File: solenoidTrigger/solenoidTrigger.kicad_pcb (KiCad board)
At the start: 2 copper layers, 88.9 x 88.9 mm, 45 parts, among them J8 CONN_02X03, P1 OSTTC03, P2 OSTTC02, P3 OSTTC08, P4 OSTTC03, P5 OSTTC03, Q1 NMOS_CDS16, Q2 NMOS_CDS16, Q3 NMOS_CDS16, Q4 NMOS_CDS16, Q5 NMOS_CDS16, Q6 NMOS_CDS16, U1 L78M05CDT-TR, U2 ATmega328P-AU, Y2 Crystal_SMD

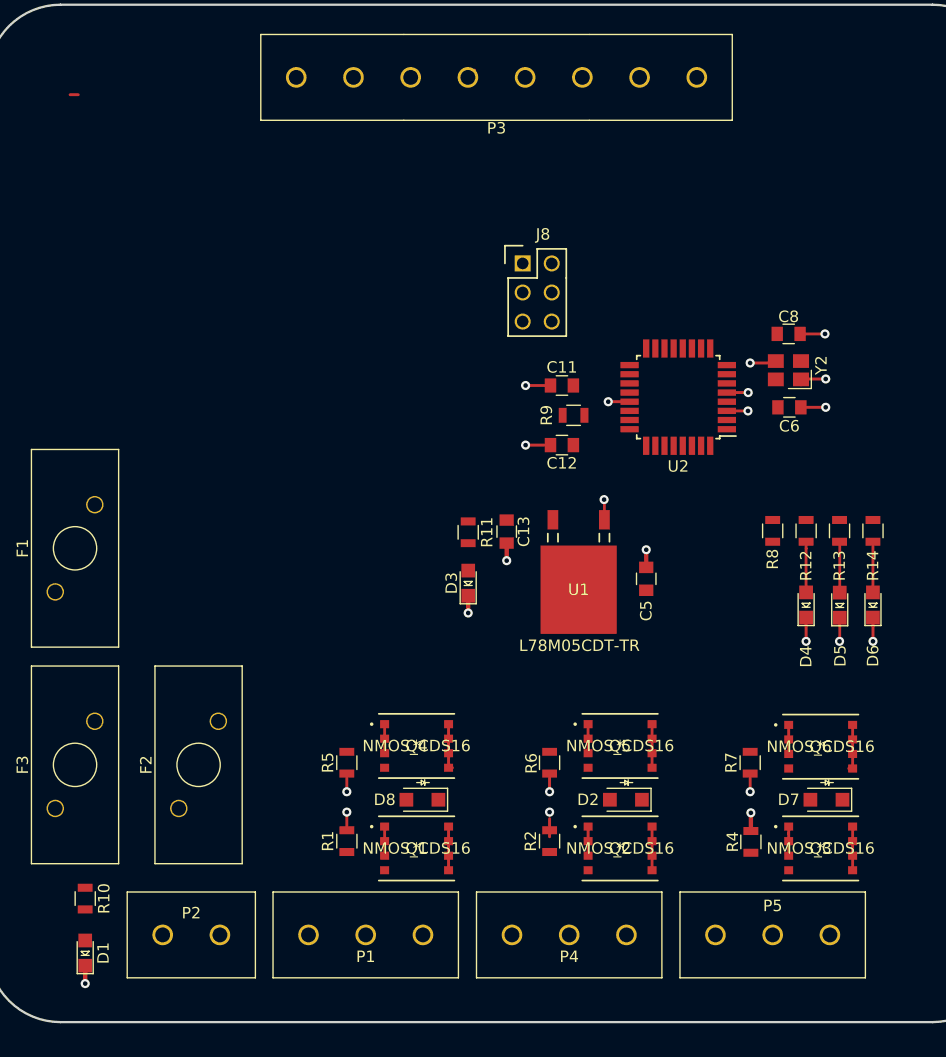
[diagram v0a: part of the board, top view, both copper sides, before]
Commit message: global deletion of all tracks so I can replace all of them
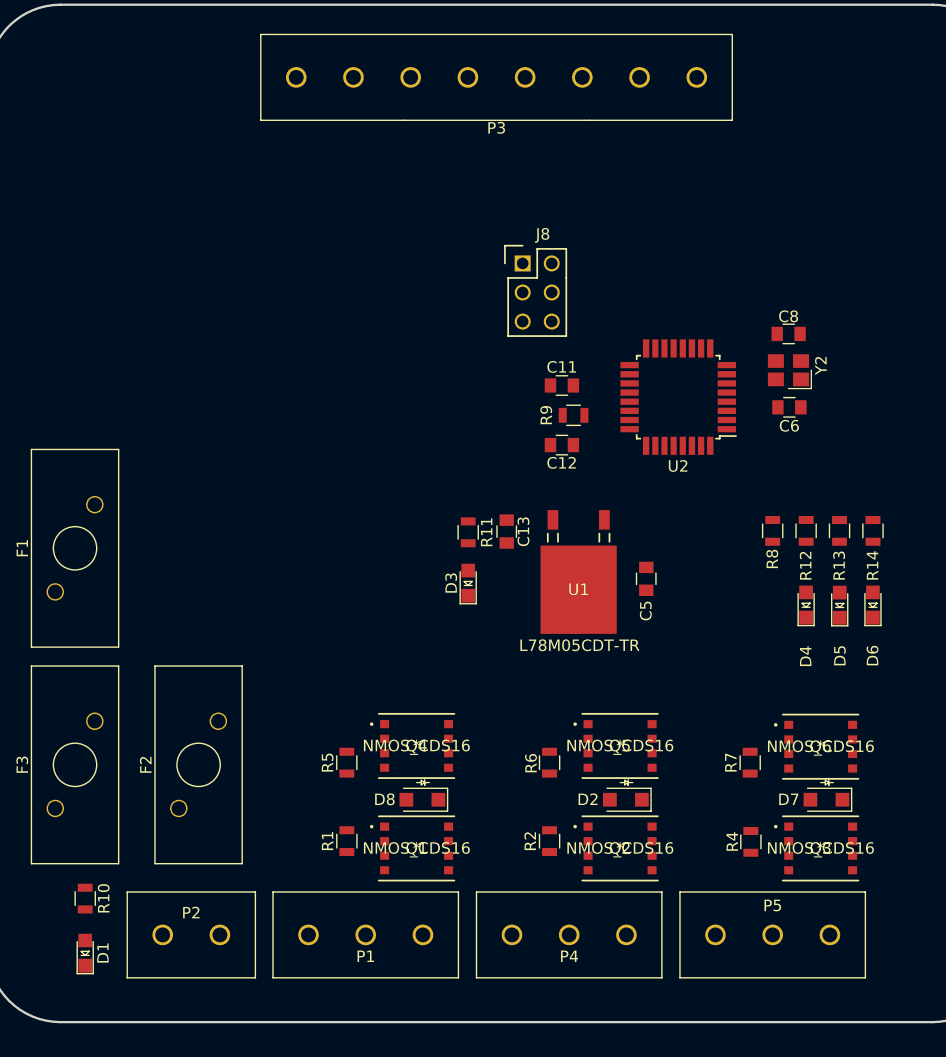
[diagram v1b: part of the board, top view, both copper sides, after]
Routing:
- net GND: track 43.3 -> 0.00 mm, vias 23 -> 0
- net /12V_Switch: track 23.7 -> 0.00 mm
- net /12V_Solenoid3: track 5.08 -> 0.00 mm
- net /12V_Solenoid2: track 5.08 -> 0.00 mm
- net /12V_Solenoid1: track 5.08 -> 0.00 mm
- net Net-(D5-Pad2): track 4.79 -> 0.00 mm
- net Net-(D6-Pad2): track 4.43 -> 0.00 mm
- net Net-(D4-Pad2): track 4.43 -> 0.00 mm
- net /MISO: track 1.41 -> 0.00 mm
- net (no net): track 0.72 -> 0.00 mm
- net VCC: track 0.58 -> 0.00 mm
- net /ctrl_pin_1-2: track 0.53 -> 0.00 mm
- net /PLED3: track 0.53 -> 0.00 mm

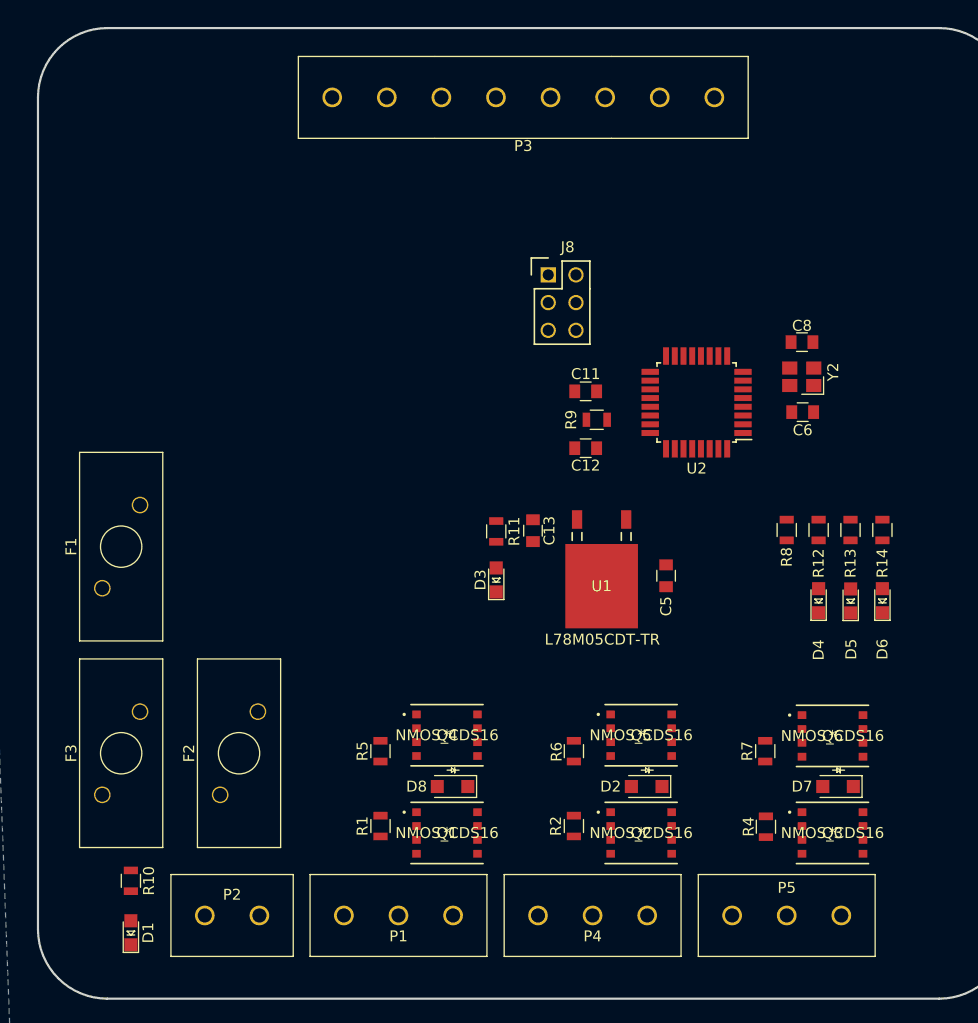
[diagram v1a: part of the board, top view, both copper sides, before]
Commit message: placed down about half the traces
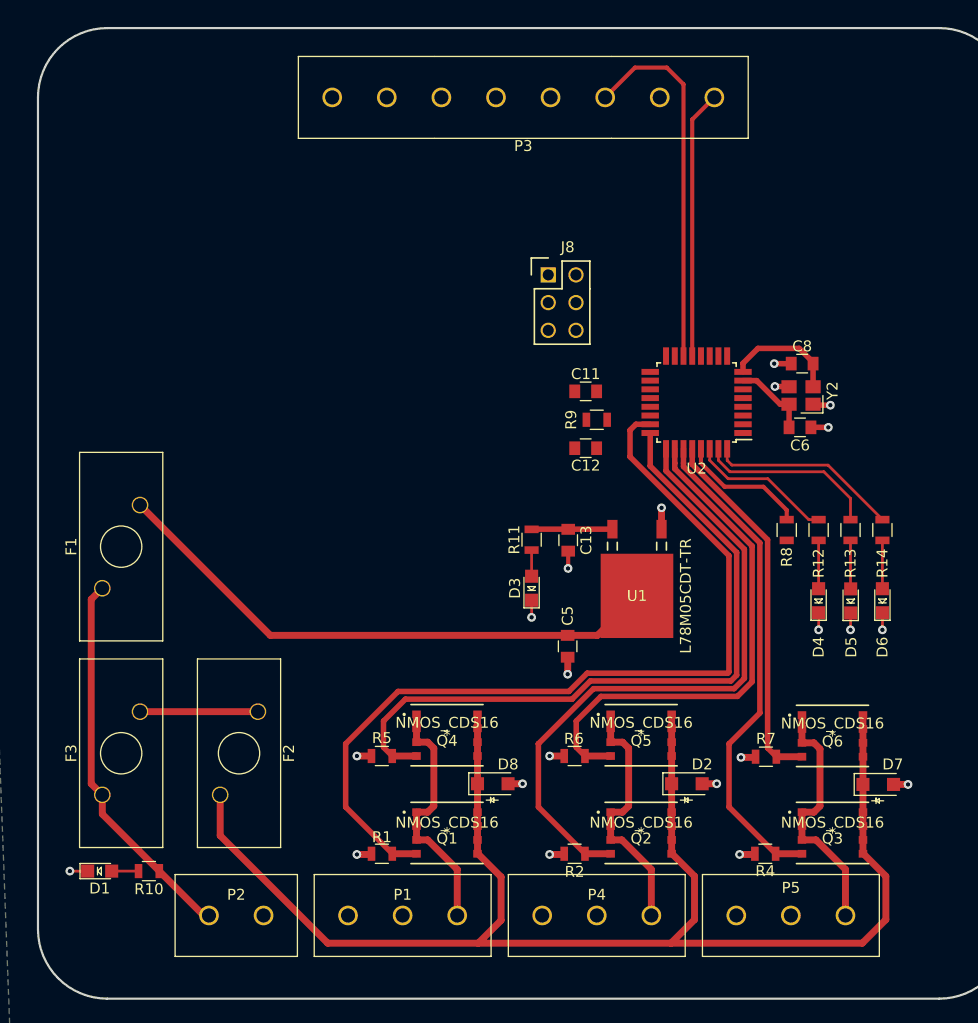
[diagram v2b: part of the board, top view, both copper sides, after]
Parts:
- moved F2 22.4 mm to (121.3, 127.1), turned to 180 degrees
- moved C5 11.1 mm to (151.4, 106.2), turned to 90 degrees
- moved D1 6.33 mm to (108.5, 126.7), turned to 0 degrees
- moved D2 3.69 mm to (162.3, 118.7), turned to 0 degrees
- moved D8 3.69 mm to (144.5, 118.7), turned to 0 degrees
- moved D7 3.69 mm to (179.8, 118.8), turned to 0 degrees
- moved U1 3.36 mm to (157.7, 101.5)
- moved C13 3.34 mm to (151.4, 96.4)
- moved D3 3.33 mm to (148.1, 100.8)
- moved R11 3.33 mm to (148.1, 96.4)
- moved R1 2.54 mm to (134.4, 125.2), turned to 180 degrees
- moved R2 2.54 mm to (152.0, 125.2), turned to 180 degrees
- moved R4 2.48 mm to (169.5, 125.2), turned to 180 degrees
- moved C8 1.97 mm to (172.9, 80.3), turned to 180 degrees
- moved R10 1.88 mm to (113.0, 126.7), turned to 180 degrees
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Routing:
- net /12V_Switch: track 0.00 -> 134.8 mm
- net /ctrl_pin_1-1: track 0.00 -> 79.9 mm
- net /ctrl_pin_1-2: track 0.00 -> 65.3 mm
- net /ctrl_pin_2-1: track 0.00 -> 59.5 mm
- net /12V_Low: track 0.00 -> 52.0 mm
- net /ctrl_pin_2-2: track 0.00 -> 47.8 mm
- net /ctrl_pin_3-1: track 0.00 -> 45.3 mm
- net /Source(12V): track 0.00 -> 35.1 mm
- net /CS: track 0.00 -> 33.8 mm
- net /ctrl_pin_3-2: track 0.00 -> 33.7 mm
- net GND: track 0.00 -> 31.3 mm, vias 0 -> 21
- net /G0(IRQ): track 0.00 -> 24.5 mm
- net /12V_Solenoid1: track 0.00 -> 23.1 mm
- net /12V_Solenoid2: track 0.00 -> 23.1 mm
- net /12V_Solenoid3: track 0.00 -> 23.0 mm
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
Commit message: first pass done pending approval
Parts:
- added REF**: Mounting_Hole_4-40, footprints:Mounting_Hole_4-40, F.Cu at (114.8, 44.5)
- added REF**: Mounting_Hole_4-40, footprints:Mounting_Hole_4-40, F.Cu at (184.4, 131.2)
- added REF**: Mounting_Hole_4-40, footprints:Mounting_Hole_4-40, F.Cu at (184.4, 56.9)
- added REF**: Mounting_Hole_4-40, footprints:Mounting_Hole_4-40, F.Cu at (110.5, 131.2)
- moved D3 0.38 mm to (148.5, 100.8)
- moved R11 0.38 mm to (148.5, 96.4)
- moved C13 0.25 mm to (151.7, 96.4)
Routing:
- net VCC: track 7.41 -> 160.0 mm, vias 0 -> 8
- net /RESET: track 11.8 -> 125.5 mm, vias 0 -> 4
- net /SCK: track 0.00 -> 52.0 mm
- net /MISO: track 0.00 -> 50.9 mm
- net /MOSI: track 0.00 -> 41.5 mm, vias 0 -> 2
- net GND: track 31.3 -> 39.9 mm, vias 21 -> 26
- net Net-(C11-Pad2): track 0.00 -> 8.31 mm

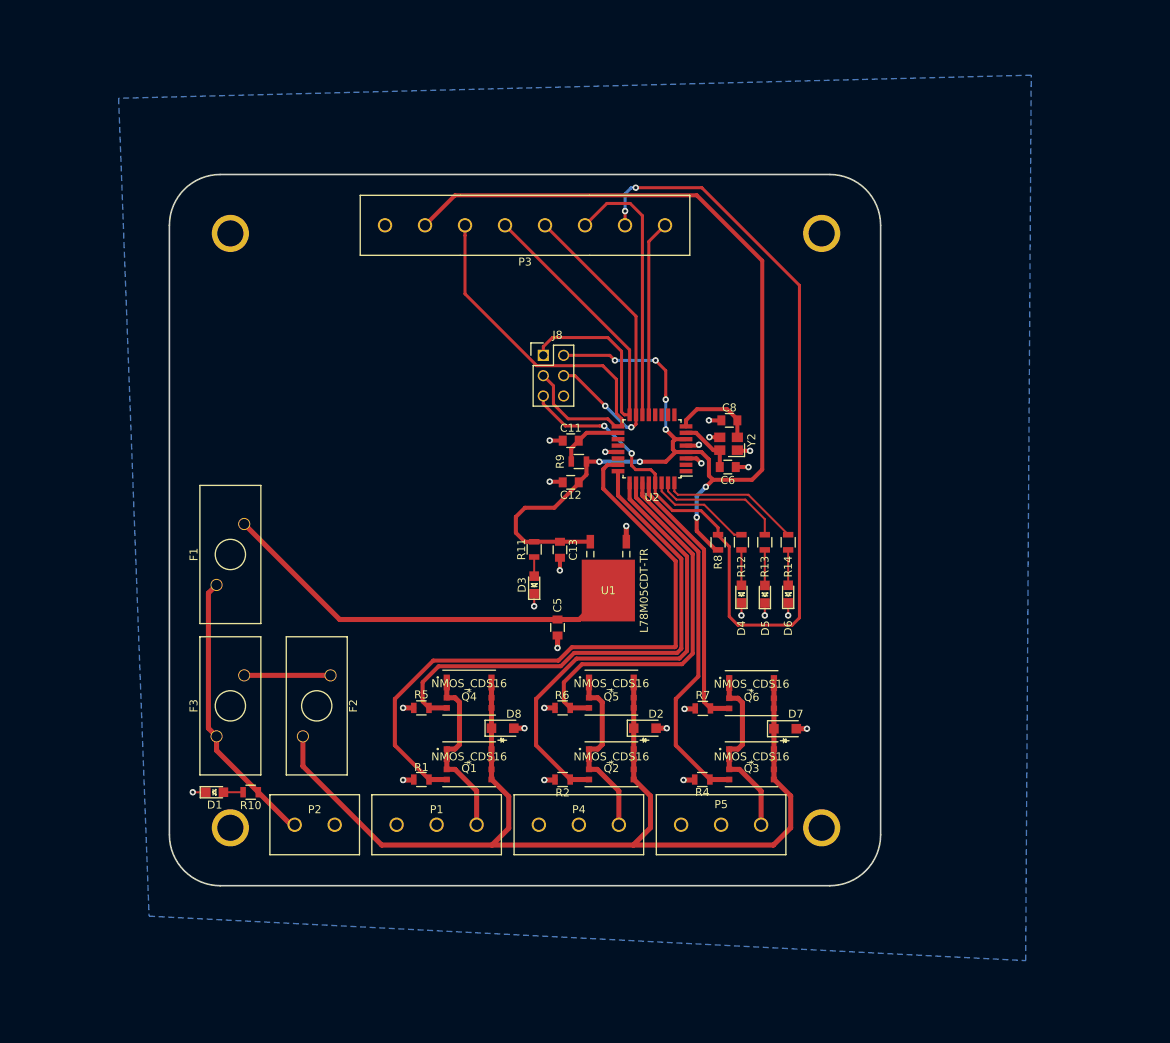
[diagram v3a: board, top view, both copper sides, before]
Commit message: added another LED, changed some pins, changed flybacks
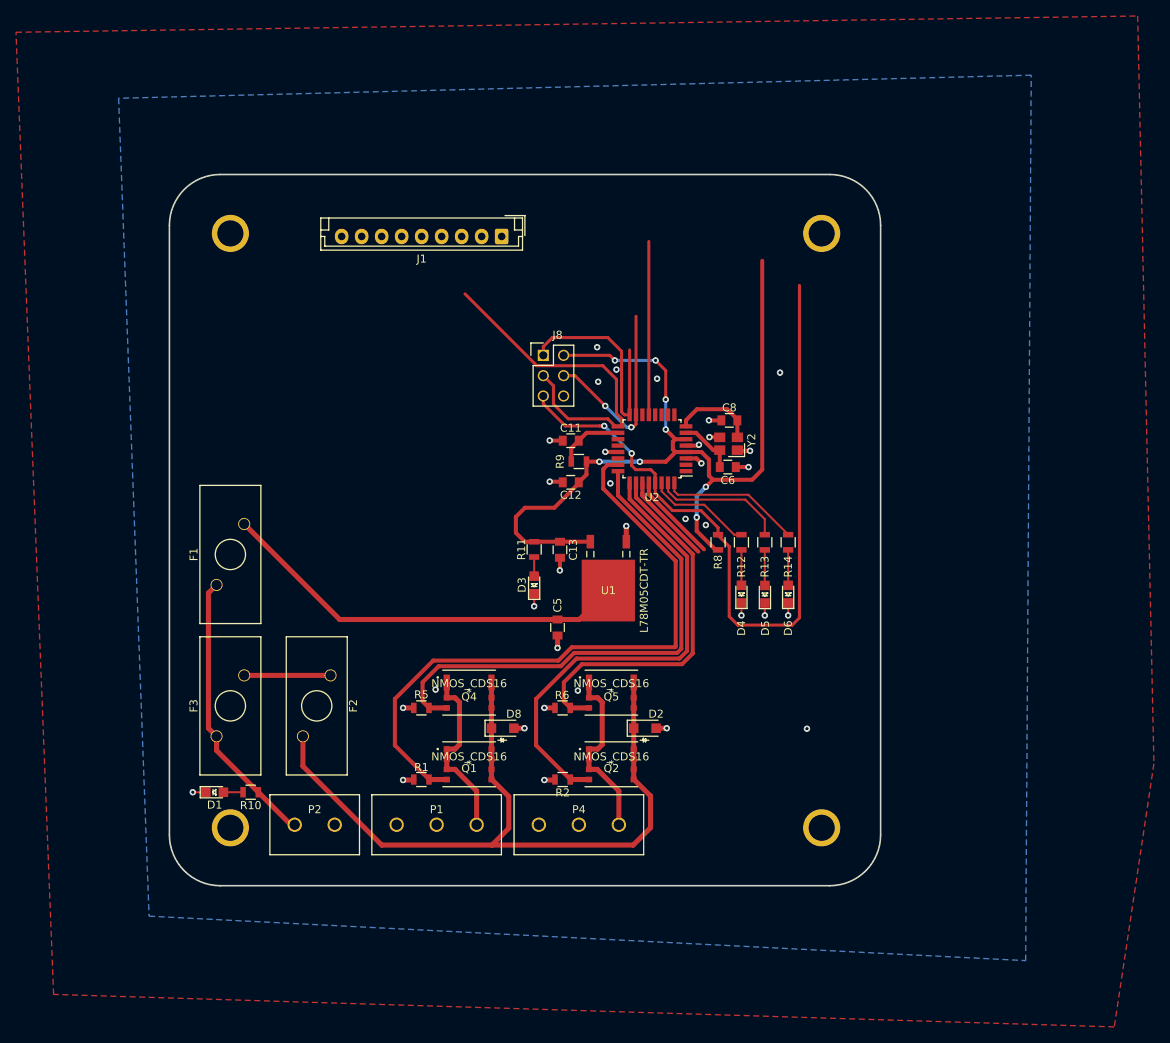
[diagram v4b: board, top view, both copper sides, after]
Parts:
- removed D7: SS110LW, footprints:D_SOD-123W_OEM
- removed P3: OSTTC08, footprints:OSTTC080162
- removed P5: OSTTC03, footprints:OSTTC030162
- removed Q3, Q6: NMOS_CDS16, footprints:CSD16322Q5
- removed R4, R7: R_1K, footprints:R_0805_OEM
- added J1: Conn_01x09_Female, Connector_JST:JST_EH_B9B-EH-A_1x09_P2.50mm_Vertical, F.Cu at (144.4, 57.3)
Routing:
- net VCC: track 160.0 -> 112.9 mm
- net /12V_Switch: track 134.8 -> 94.6 mm
- net /CS: track 33.8 -> 0.00 mm
- net /ctrl_pin_3-1: track 45.3 -> 11.5 mm
- net /RESET: track 125.5 -> 94.4 mm, vias 4 -> 2
- net /12V_Solenoid3: track 23.0 -> 0.00 mm
- net /ctrl_pin_3-2: track 33.7 -> 11.2 mm
- net /MISO: track 50.9 -> 28.9 mm
- net /MOSI: track 41.5 -> 25.4 mm
- net /SCK: track 52.0 -> 43.4 mm
- net GND: track 39.9 -> 35.9 mm, vias 26 -> 34
- net /G0(IRQ): track 24.5 -> 21.7 mm
- added copper zone on F.Cu, net GND

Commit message: removed switch
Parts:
- removed F2: 01530008Z, footprints:01530008Z
- added D7: LED_0805, footprints:LED_0805_OEM, F.Cu at (184.8, 101.3)
- added R3: R_499, footprints:R_0805_OEM, F.Cu at (184.8, 96.8)
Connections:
- net /ctrl_pin_3-1 renamed Net-(U2-Pad27)
- net /ctrl_pin_3-2 renamed Net-(U2-Pad28)
- D2 pad 1: /12V_Switch -> /12V_Solenoid2
- D8 pad 1: /12V_Switch -> /12V_Solenoid1
- F3 pad 1: /12V_High -> /12V_Switch
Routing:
- net /12V_High: track 11.1 -> 0.00 mm
- net /12V_Switch: track 94.6 -> 103.2 mm
- net GND: vias 34 -> 33
